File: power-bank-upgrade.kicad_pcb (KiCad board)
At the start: 2 copper layers, 20 x 18 mm, 26 parts, among them J1 USB_B_Micro, J2 USB_A, SW1 SW_Push, U1 MP2632B

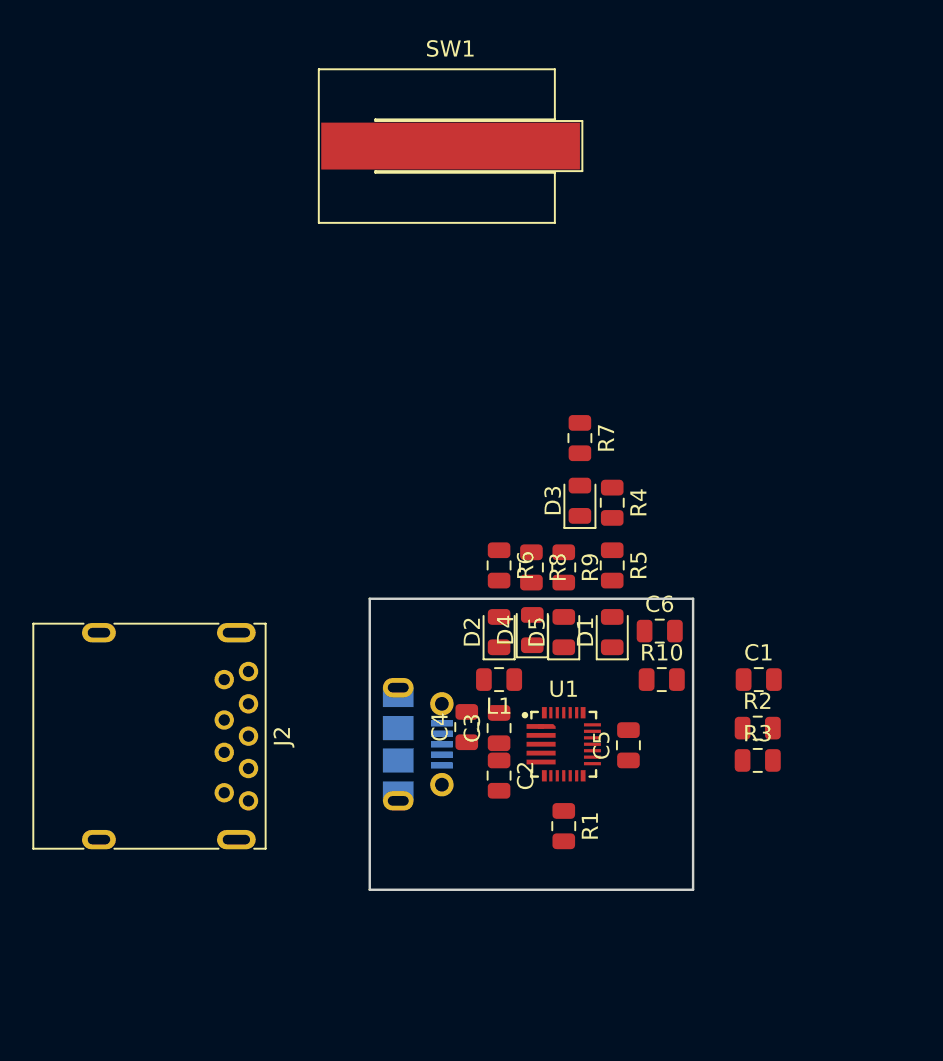
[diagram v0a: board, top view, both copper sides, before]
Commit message: Added Samtec USB Type A portm started routing
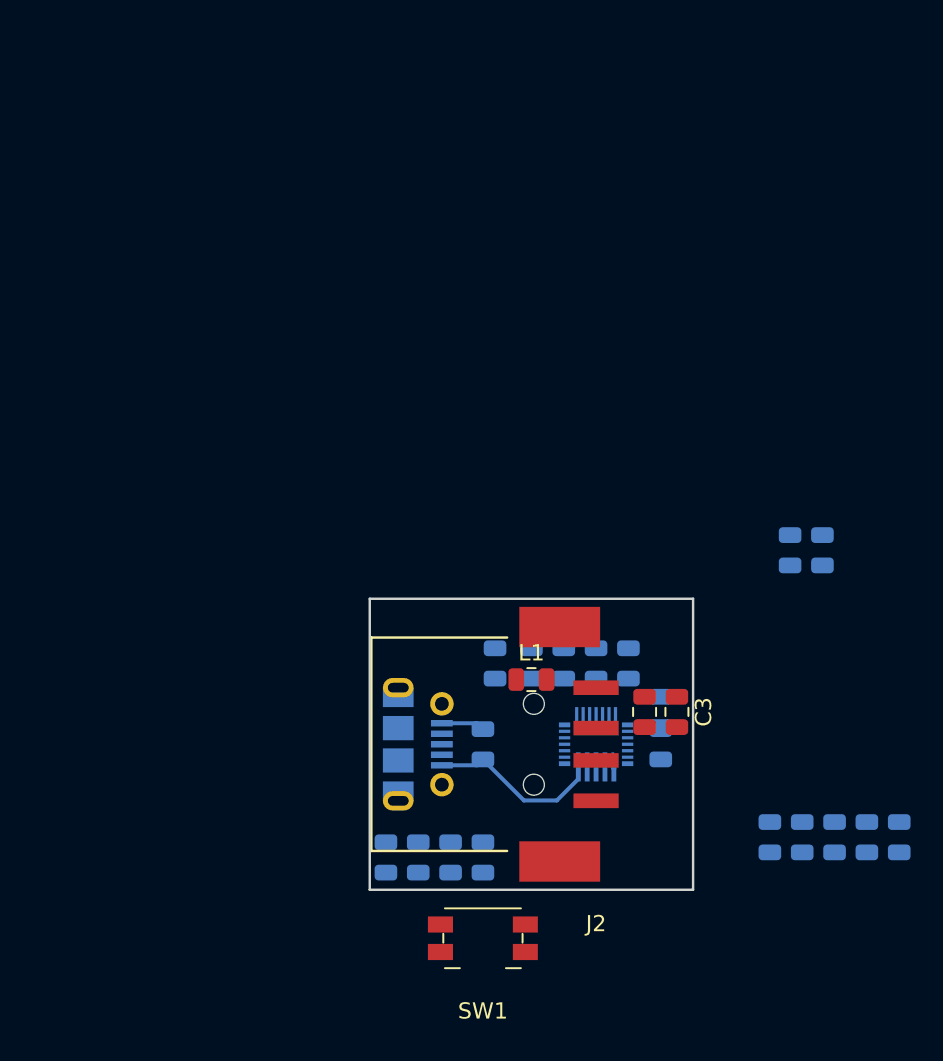
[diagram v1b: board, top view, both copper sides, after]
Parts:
- C1, C2, C5, C6, D1, D2, D3, D4, D5, R1, R10, R2, R3, R4, R5, R6, R7, R8, R9, U1: moved to B.Cu
- J2: footprint Connector_USB:USB3_A_Molex_48393-001 -> power-bank:USB_A_Samtec_USB-A-S-F-B-SM2.kicad_mod
- SW1: footprint Battery:BatteryHolder_Keystone_2993 -> Button_Switch_SMD:Panasonic_EVQPUJ_EVQPUA
- moved SW1 49.0 mm to (27.0, 193.0), turned to 180 degrees
- moved R4 27.3 mm to (52.8, 186.8), turned to 90 degrees
- moved R6 23.7 mm to (44.8, 186.8)
- moved R8 23.6 mm to (46.8, 186.8)
- moved R9 23.6 mm to (48.8, 186.8)
- moved J2 23.3 mm to (34.0, 181.0), turned to 0 degrees
- moved R5 23.0 mm to (50.8, 186.8)
- moved R7 16.5 mm to (48.0, 169.0)
- moved D1 16.1 mm to (27.0, 188.0)
- moved D4 15.7 mm to (23.0, 188.0)
- moved D2 15.6 mm to (21.0, 188.0)
- moved D5 15.6 mm to (25.0, 188.0)
- moved R3 13.4 mm to (32.0, 176.0), turned to 90 degrees
- moved D3 13.4 mm to (46.0, 169.0), turned to 270 degrees
- moved C3 11.0 mm to (39.0, 179.0), turned to 270 degrees
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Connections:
- J1 pad 4: Net-(J1-Pad4) -> (no net)
- U1 pad 20: Net-(U1-Pad20) -> (no net)
- U1 pad 3: (no net) -> Net-(C3-Pad1)
- U1 pad 4: (no net) -> Net-(C3-Pad1)
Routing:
- net Net-(C2-Pad1): track 0.00 -> 10.9 mm
- net GNDA: track 0.00 -> 2.69 mm
- added copper zone on B.Cu, net GNDA
- added copper zone on F.Cu, net GNDA

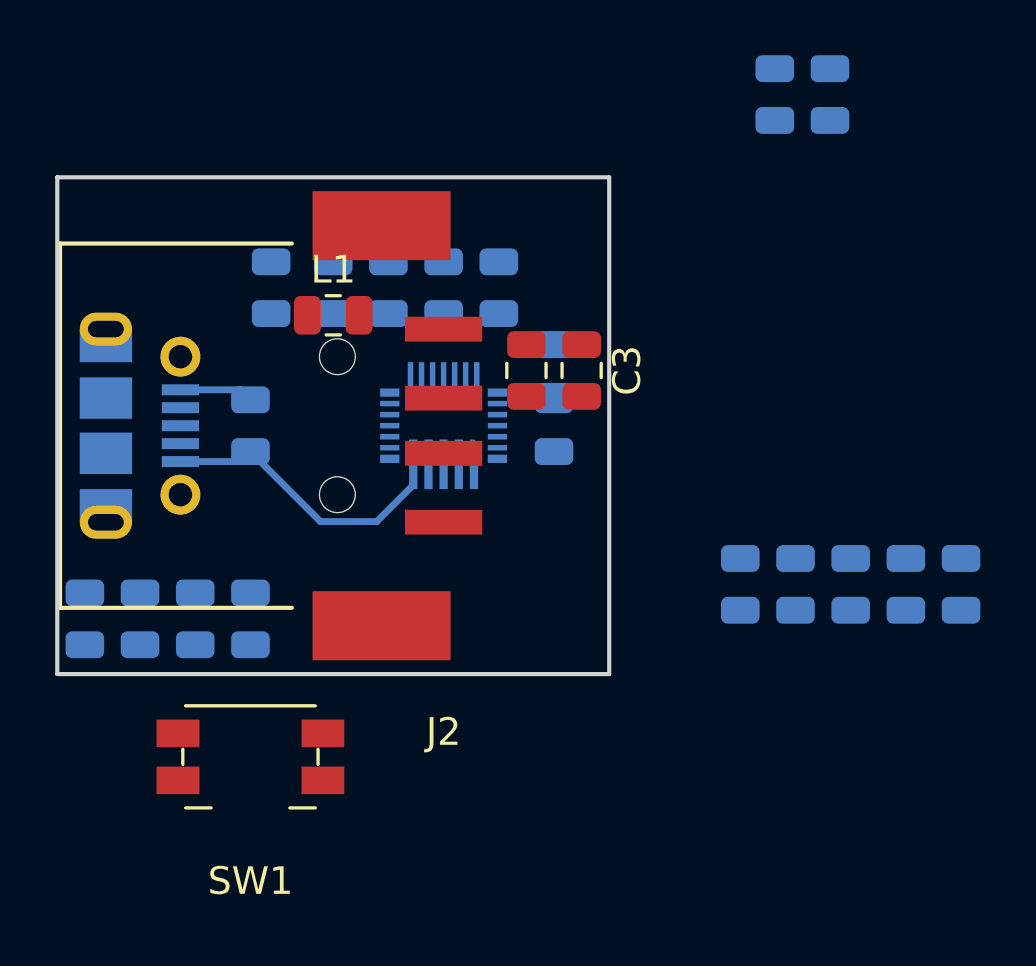
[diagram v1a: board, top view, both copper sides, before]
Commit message: Completed routing for v1. Added fp-info-cache to .gitignore
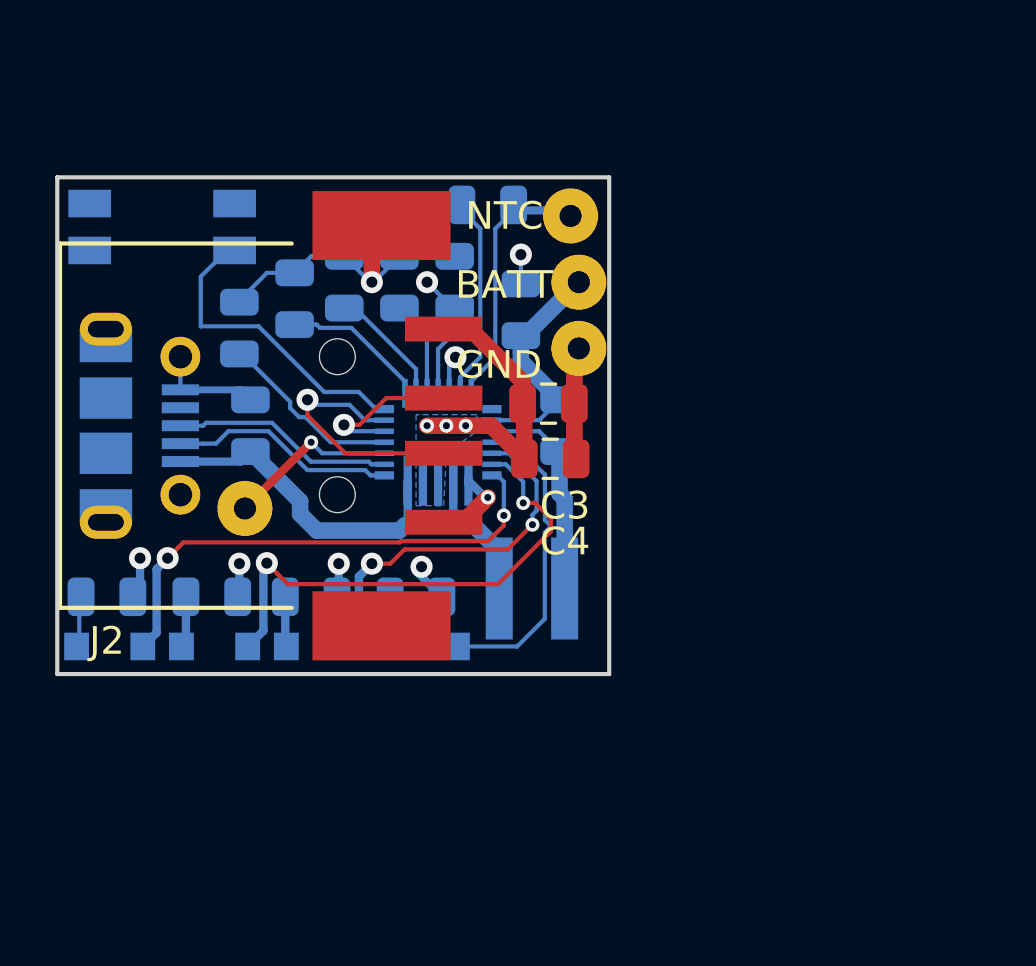
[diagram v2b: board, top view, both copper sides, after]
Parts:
- removed D1: LED, LED_SMD:LED_0805_2012Metric
- removed R5: R, Resistor_SMD:R_0805_2012Metric
- added BATT: Conn_01x01_Female, Connector_Wire:SolderWirePad_1x01_Drill0.8mm, F.Cu at (38.9, 175.8)
- added GND: Conn_01x01_Female, Connector_Wire:SolderWirePad_1x01_Drill0.8mm, F.Cu at (38.9, 178.2)
- added J6: Conn_01x01_Female, Connector_Wire:SolderWirePad_1x01_Drill0.8mm, F.Cu at (26.8, 184.0)
- added NTC: Conn_01x01_Female, Connector_Wire:SolderWirePad_1x01_Drill0.8mm, F.Cu at (38.6, 173.4)
- D2, D3, D4, D5: footprint LED_SMD:LED_0805_2012Metric -> power-bank:APA2107
- L1: footprint Inductor_SMD:L_0805_2012Metric -> Inductor_SMD:L_Wuerth_MAPI-4020; moved to B.Cu
- R6, R7, R8, R9: value R -> 210
- SW1: moved to B.Cu
- moved R7 28.9 mm to (25.6, 187.2), turned to 180 degrees
- moved D3 28.5 mm to (25.7, 189.0), turned to 180 degrees
- moved R6 23.0 mm to (21.8, 187.2), turned to 180 degrees
- moved SW1 19.5 mm to (23.8, 173.8)
- moved R8 17.6 mm to (29.2, 187.2), turned to 180 degrees
- moved R9 15.8 mm to (33.0, 187.2), turned to 180 degrees
- moved R4 15.6 mm to (38.2, 181.0), turned to 270 degrees
- moved L1 12.2 mm to (37.2, 186.9)
- moved D5 8.36 mm to (33.3, 189.0), turned to 180 degrees
- moved D4 6.58 mm to (29.5, 189.0), turned to 180 degrees
- moved R10 6.46 mm to (35.6, 173.0), turned to 180 degrees
- moved C6 4.37 mm to (36.8, 176.8), turned to 90 degrees
- moved C4 3.31 mm to (37.9, 182.2), turned to 0 degrees
- moved R1 1.86 mm to (26.6, 177.5)
- moved C3 1.70 mm to (37.8, 180.2), turned to 0 degrees
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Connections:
- J1 pad 4: (no net) -> Net-(J1-Pad4)
- U1 pad 20: (no net) -> Net-(U1-Pad20)
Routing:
- net GNDA: track 2.69 -> 29.0 mm, vias 0 -> 4
- net Net-(D3-Pad1): track 0.00 -> 18.6 mm, vias 0 -> 2
- net Net-(D2-Pad1): track 0.00 -> 18.4 mm, vias 0 -> 2
- net Net-(D4-Pad1): track 0.00 -> 14.1 mm, vias 0 -> 2
- net Net-(SW1-Pad2): track 0.00 -> 11.3 mm
- net Net-(D5-Pad1): track 0.00 -> 11.1 mm
- net Net-(C3-Pad1): track 0.00 -> 10.5 mm, vias 0 -> 3
- net VCC: track 0.00 -> 10.1 mm, vias 0 -> 5
- net /NTC+: track 0.00 -> 9.41 mm
- net Net-(J2-Pad3): track 0.00 -> 9.16 mm, vias 0 -> 1
- net /VBATT: track 0.00 -> 8.67 mm
- net Net-(J1-Pad2): track 0.00 -> 8.24 mm
- net Net-(J1-Pad3): track 0.00 -> 8.05 mm
- net Net-(L1-Pad2): track 0.00 -> 7.79 mm
- net /VNTC: track 0.00 -> 7.20 mm
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- added copper zone on In1.Cu, net GNDA
- added copper zone on B.Cu, net Net-(C3-Pad1)
- added copper zone on In2.Cu, net VCC
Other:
- copper layers 2 -> 4
- net class Default: clearance 0.2 -> 0.1524; trace_width 0.25 -> 0.1524; via_dia 0.8 -> 0.508; via_drill 0.4 -> 0.254
- rule pad_to_mask_clearance: 0.051 -> 0.0508
- rule trace_clearance: 0.2 -> 0.1524
- rule trace_min: 0.2 -> 0.1524
- rule via_min_drill: 0.3 -> 0.254
- rule via_min_size: 0.4 -> 0.508
